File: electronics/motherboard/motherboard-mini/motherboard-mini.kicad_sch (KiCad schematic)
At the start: 41 parts, among them J1 JTAG, J12 JTAG, J3 2604-3102, J5 USB4070-30-C_REVC5, Q1 MMDT3904, Q2 BC847, SW1 BOOT, SW2 RESET, U1 CP2102N-Axx-xQFN28, U2 ESP32-WROOM-32E_(16MB), Y1 32.768KHz

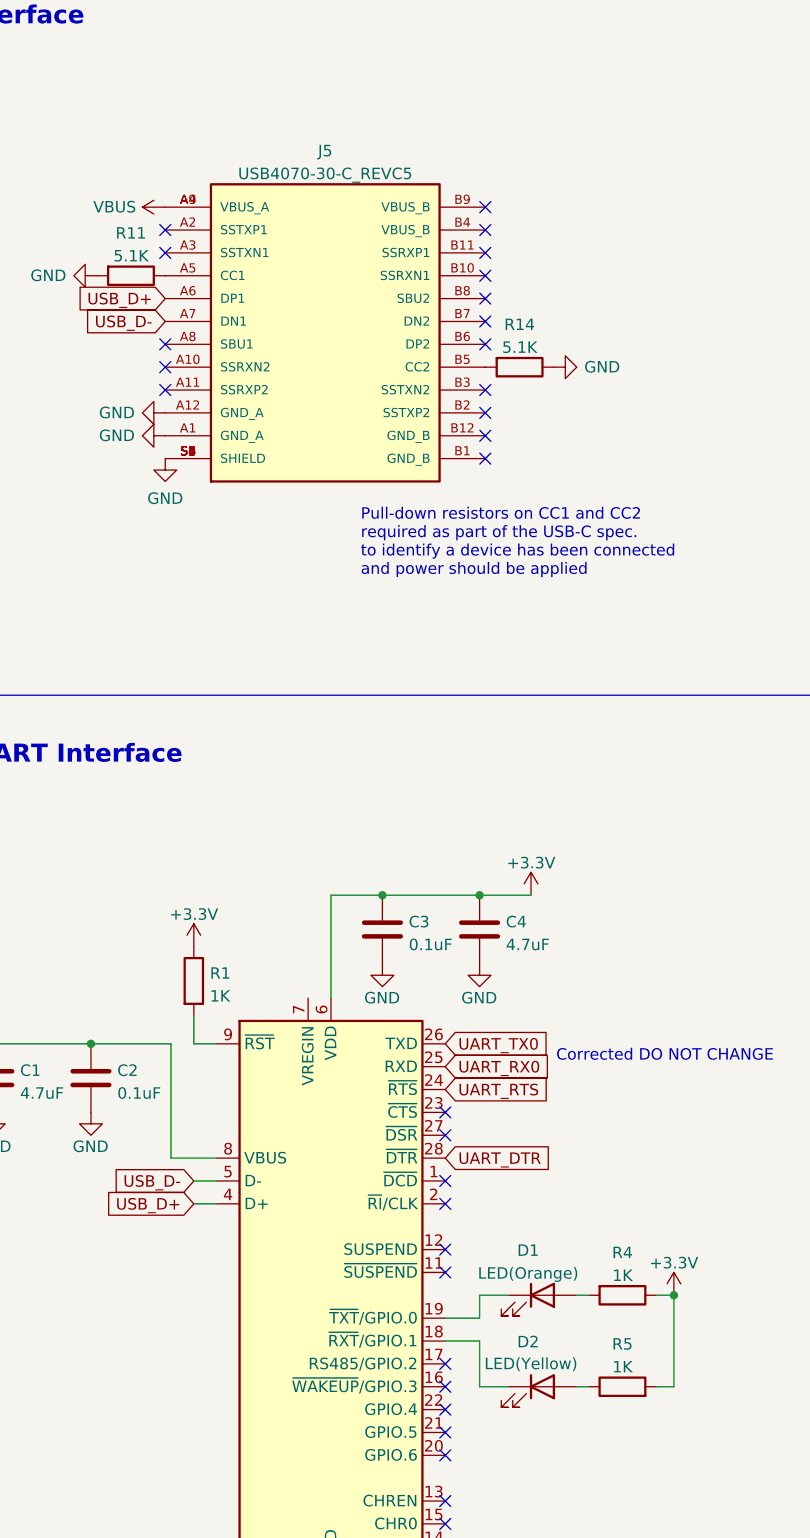
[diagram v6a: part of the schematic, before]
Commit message: added component information for all items in motherboard
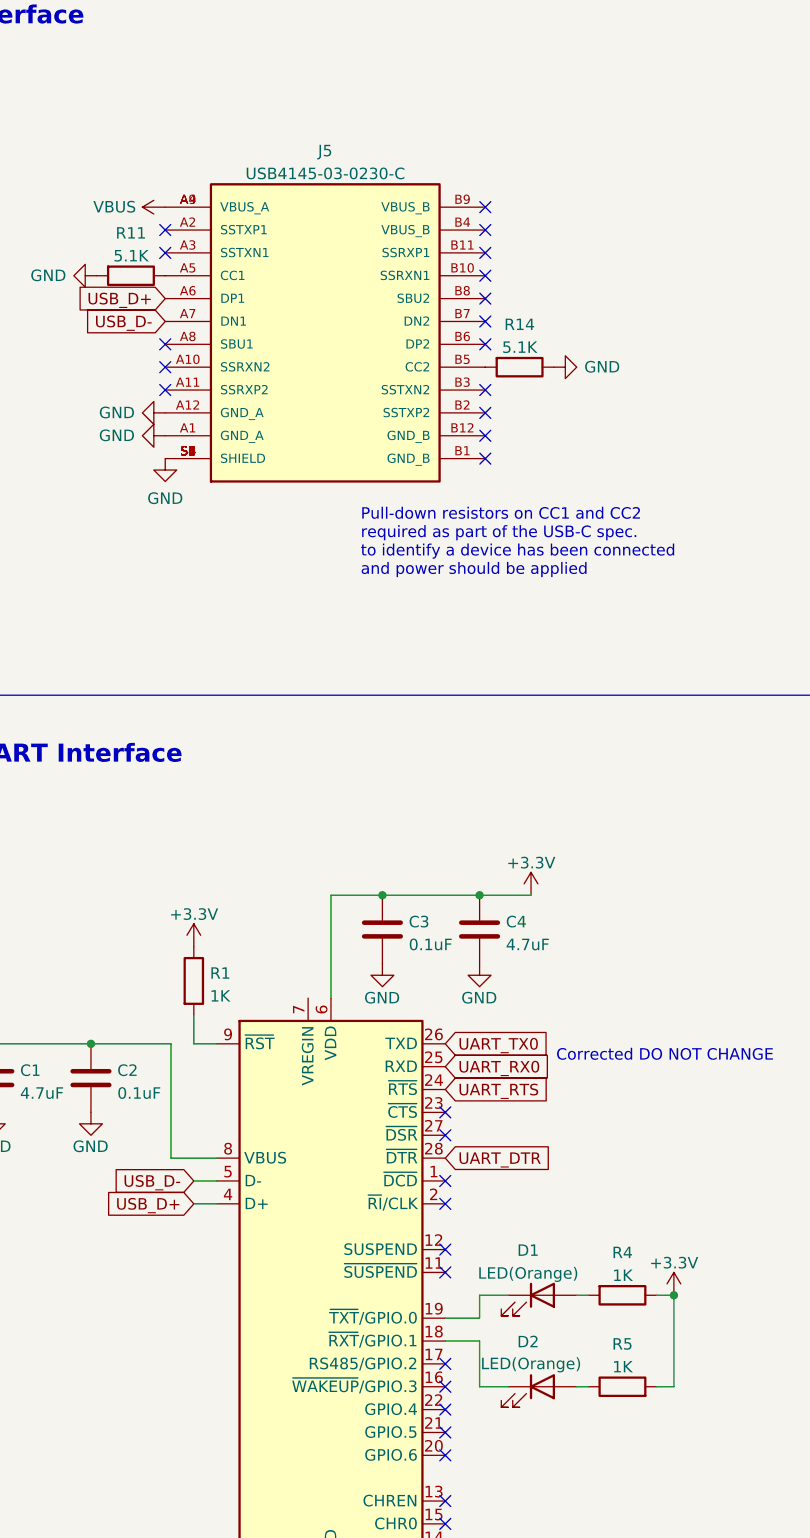
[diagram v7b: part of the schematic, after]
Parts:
- C1, C4: Part (none) -> CL21B475KOFNFNE
- C10: Part (none) -> C0805C226M8PAC7800
- C2, C3, C6, C7: Part (none) -> AC0805KRX7R7BB104
- C5: Part (none) -> C0805C105K3RAC7800
- C8, C9: Part (none) -> VJ0805A120FXJCW1BC
- D1: Part (none) -> LO R976-PS-1
- D2: value LED(Yellow) -> LED(Orange); Part (none) -> LO R976-PS-1
- J12: Part (none) -> 3221-10-0100-00
- J3: Part (none) -> 2604-3102
- J5: value USB4070-30-C_REVC5 -> USB4145-03-0230-C
- LS1: Part (none) -> PS1240P02BT
- R1, R13, R4, R5: Part (none) -> CR0805-FX-1001ELF
- R10: Part (none) -> CR0805-FW-1005ELF
- R11, R14: Part (none) -> CRCW08055K10FKEA
- R12: Part (none) -> https://www.digikey.com.au/en/products/detail/yageo/RC0805F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
- R15, R16: Part (none) -> CRG0805F4K7
- R17, R2, R3, R6, R9: Part (none) -> RC0805FR-0710KP
- R7, R8: Part (none) -> CR0805-J/-000ELF
- SW1, SW2: Part (none) -> 1977223-6
- U1: Part (none) -> CP2102N-A02-GQFN28
- U2: MANUFACTURER Espressif Systems -> (none); MAXIMUM_PACKAGE_HEIGHT 3.25mm -> (none); PARTREV 1.4 -> (none); Part (none) -> ESP32-WROOM-32E-N16; STANDARD Manufacturer Recommendations -> (none)
- Y1: Part (none) -> ABS07AIG-32.768KHZ-T

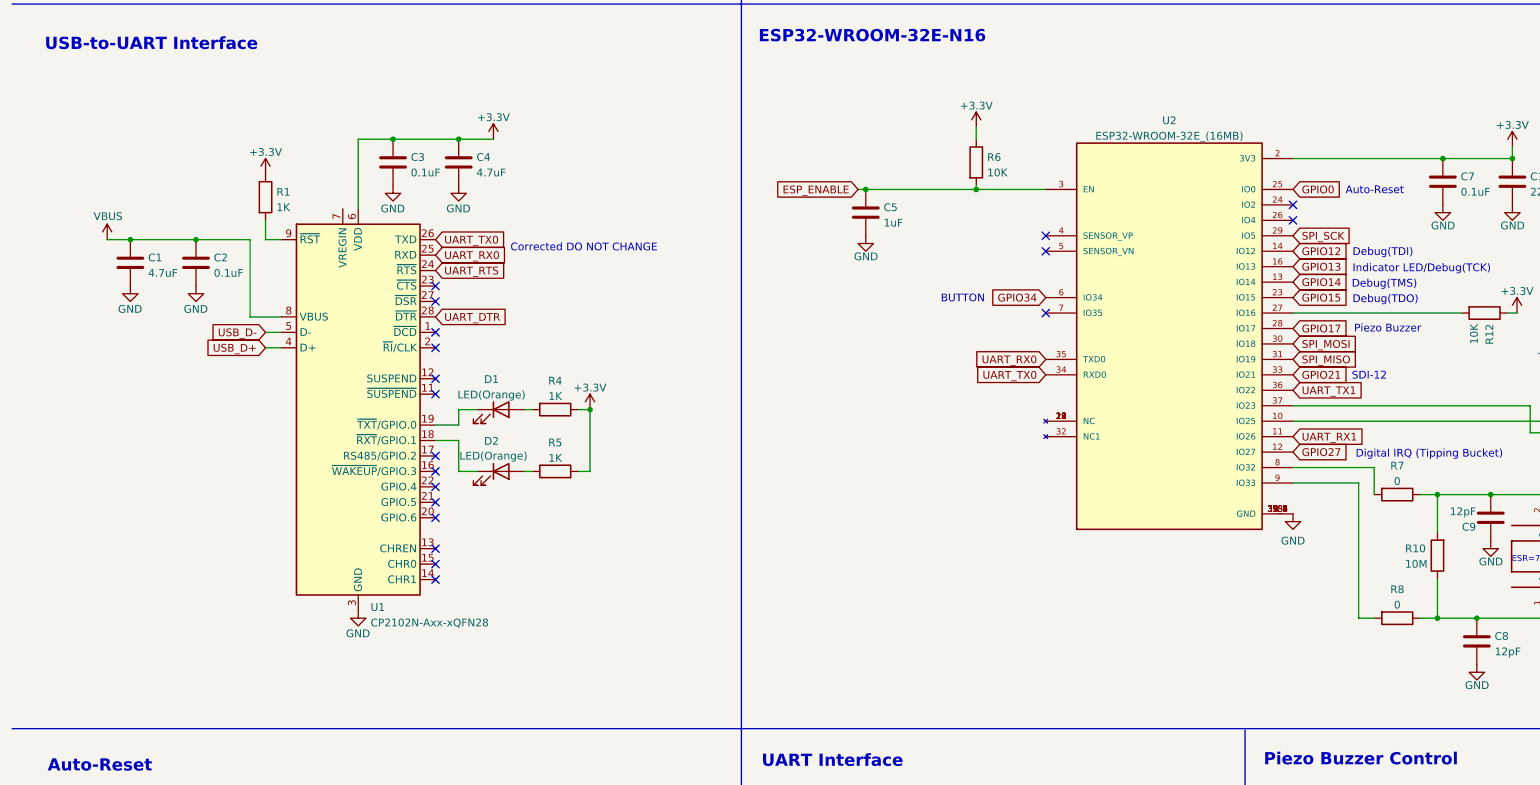
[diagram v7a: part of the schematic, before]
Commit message: updated usb-to-uart, fixed some pin label issues
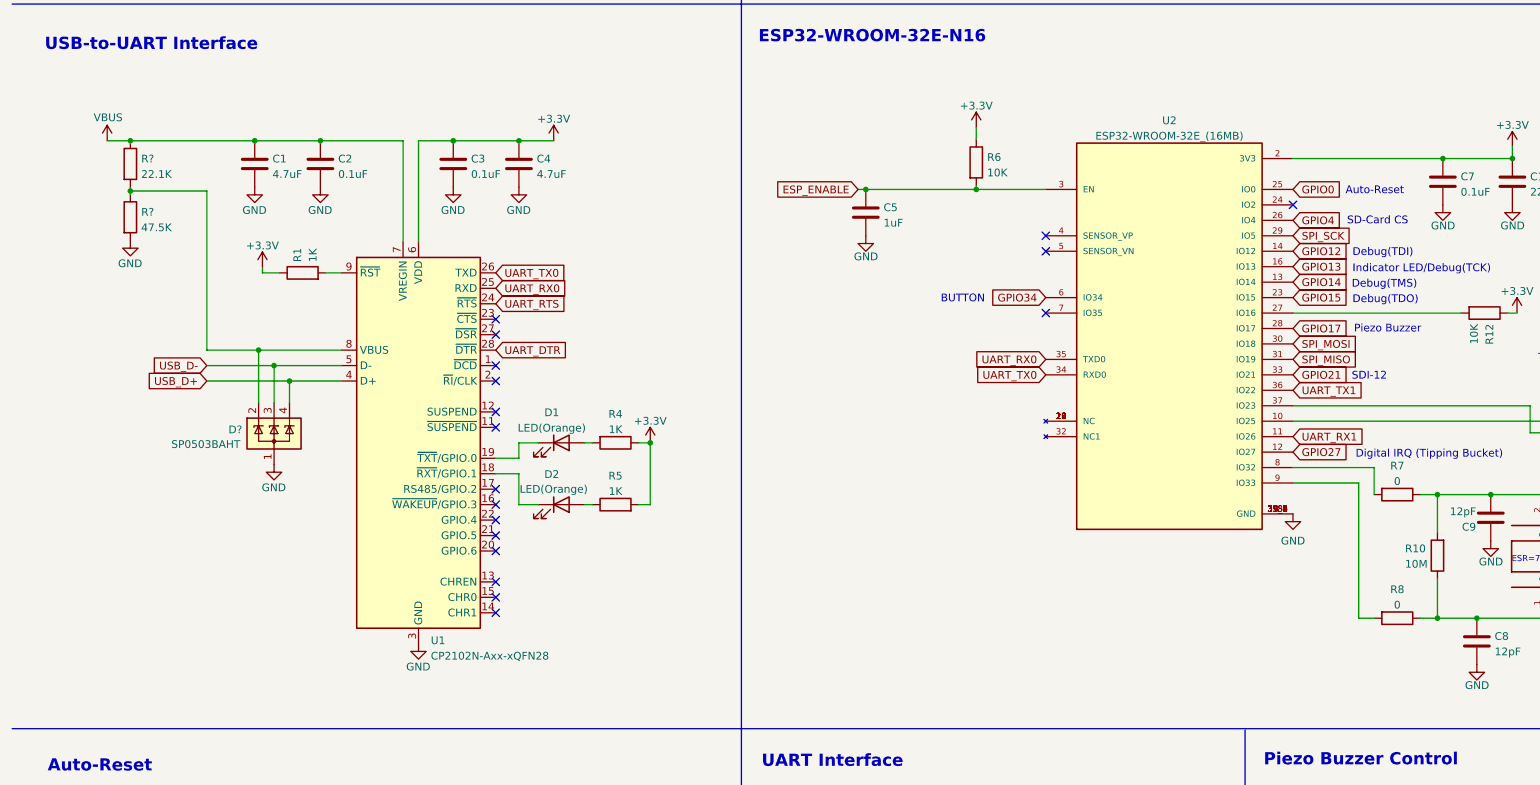
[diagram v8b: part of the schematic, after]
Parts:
- added D?: SP0503BAHT, Package_TO_SOT_SMD:SOT-143, symbol Power_Protection:SP0503BAHT
- added R?: 22.1K, Resistor_SMD:R_0805_2012Metric, symbol Device:R
- added R?: 47.5K, Resistor_SMD:R_0805_2012Metric, symbol Device:R
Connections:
- net GND: now also D?.1 (A), R?.2
- net USB_D+: now also D?.4 (K)
- net USB_D-: now also D?.3 (K)
- net VBUS: now also U1.7 (VREGIN), R?.1; no longer U1.8 (VBUS)
- net GPIO4: now reaches U2.26 (IO4)
- new net: D?.2 (K), R?.1, R?.2, U1.8 (VBUS)
- no-connect marks 40 -> 39
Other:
- note added: "SD-Card CS"
- note removed: "Corrected DO NOT CHANGE"
- moved on the sheet: C1, C2, C3, C4, D1, D2, R1, R4, R5, U1
